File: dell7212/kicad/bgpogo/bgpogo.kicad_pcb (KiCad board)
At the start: 2 copper layers, 69.4 x 99.5 mm, 22 parts, among them J1 Conn_02x13_Odd_Even, J2 USB1135-15-9-L-B_REVA1, J3 Conn_01x13, J6 Conn_01x13, J7 Conn_01x09, J8 PJ-104H, J9 Conn_01x03, U1 AZ1117-5.0

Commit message: spam
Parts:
- added REF**: KiCad-Logo2_5mm_SilkScreen, Symbol:KiCad-Logo2_5mm_SilkScreen, F.Cu at (132.3, 95.9)
- added REF**: OSHW-Logo_5.7x6mm_SilkScreen, Symbol:OSHW-Logo_5.7x6mm_SilkScreen, F.Cu at (124.0, 122.6)

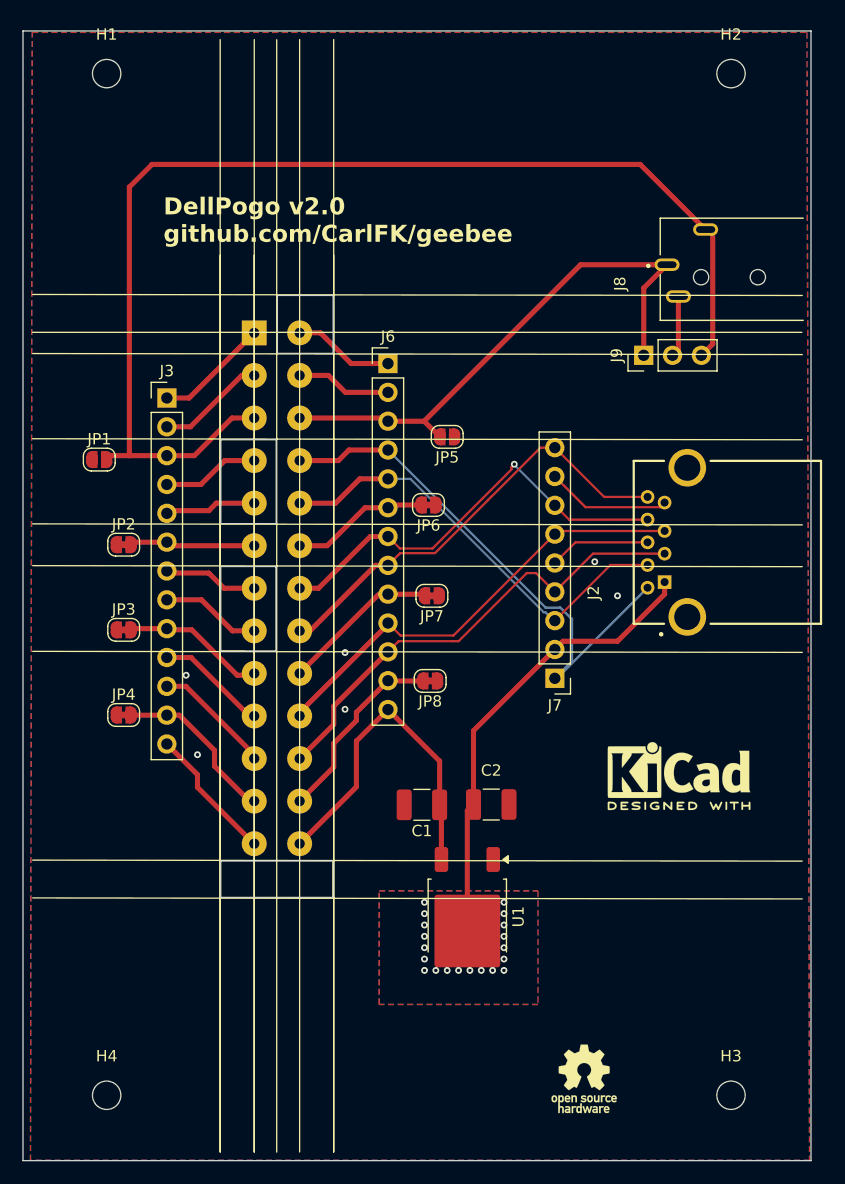
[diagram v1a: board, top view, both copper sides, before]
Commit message: better power plug lables and header placement.
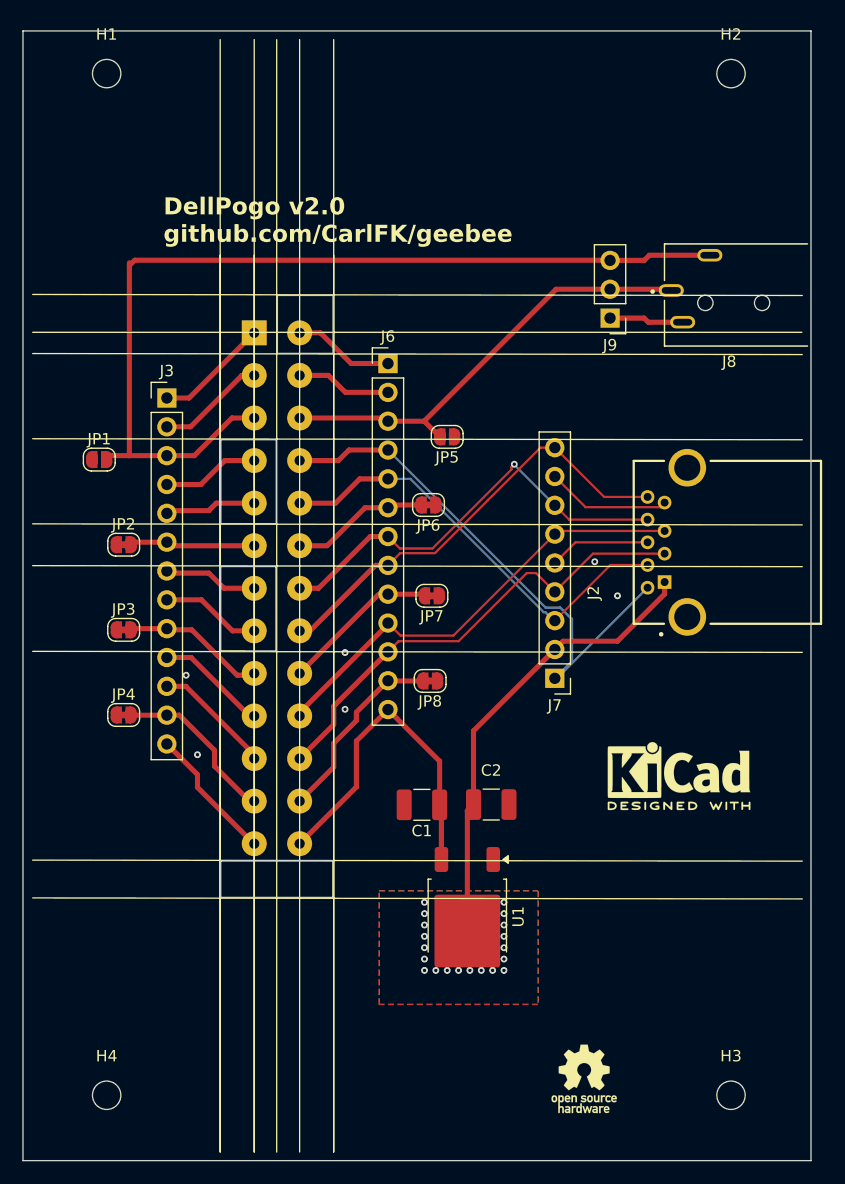
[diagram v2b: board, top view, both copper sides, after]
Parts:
- moved J9 4.42 mm to (126.3, 55.5), turned to 180 degrees
- moved J8 2.30 mm to (139.7, 54.2)
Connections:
- J8 pad 3: Net-(J9-Pin_2) -> /pj3
- J9 pad 1: /p6 -> /pj3
- J9 pad 2: Net-(J9-Pin_2) -> /p6
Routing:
- net /p5: track 103.0 -> 84.3 mm
- net /p6: track 49.1 -> 39.7 mm
- net /pj3: track 0.00 -> 6.55 mm
- net Net-(J9-Pin_2): track 5.39 -> 0.00 mm
- removed copper zone on B.Cu, net GND
- removed copper zone on F.Cu, net GND
